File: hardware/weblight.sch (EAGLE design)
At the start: 19 parts, among them U1 ATtiny85-20SU

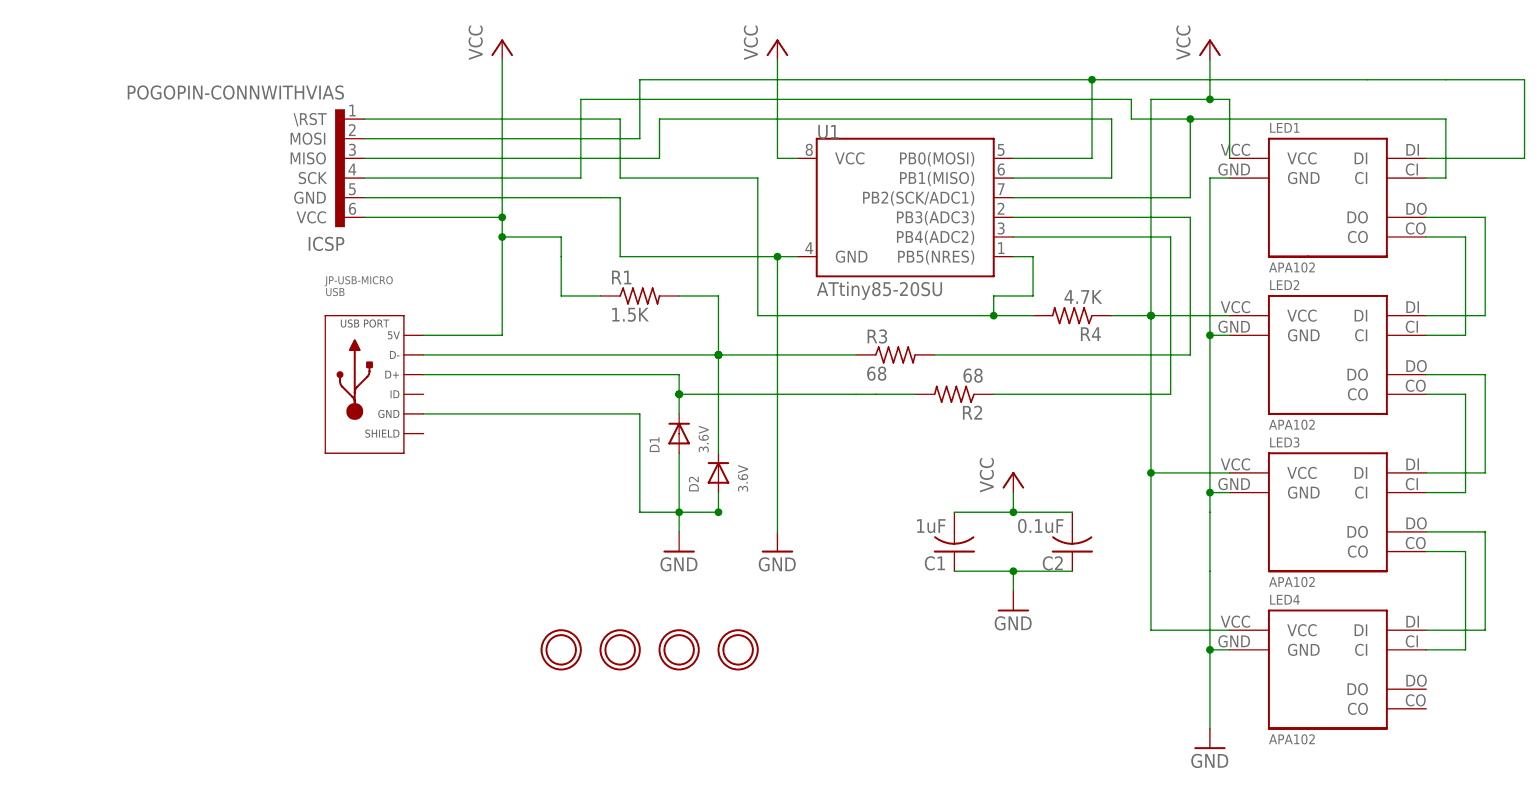
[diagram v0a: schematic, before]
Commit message: mf2 production 0805 - ordered from OSH & Seeed
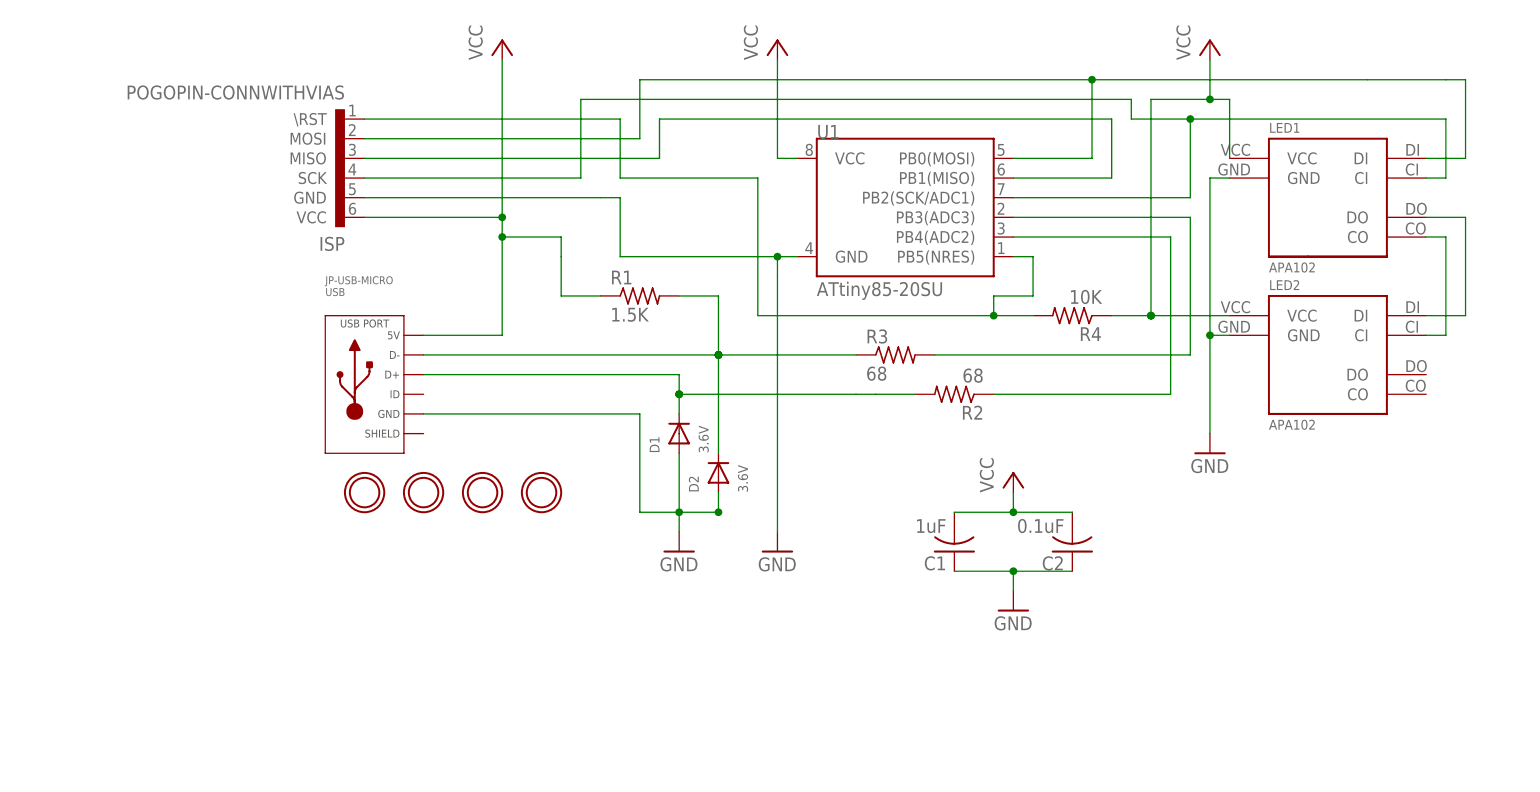
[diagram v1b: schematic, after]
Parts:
- removed LED3, LED4: APA102, weblight:APA102
- C1, C2: device rcl:C-USC0402 -> rcl:C-USC0805
- D1, D2: device microbuilder:DIODESOD-523 -> microbuilder:DIODESOD-323
- R1, R2, R3: device rcl:R-US_R0402 -> rcl:R-US_R0805
- R4: value 4.7K -> 10K; device rcl:R-US_R0402 -> rcl:R-US_R0805
- renumbered ICSP to ISP
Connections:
- removed net CLK_3: LED2.CO, LED3.CI
- removed net CLK_4: LED3.CO, LED4.CI
- removed net DIN_3: LED2.DO, LED3.DI
- removed net DIN_4: LED3.DO, LED4.DI
- net GND: no longer LED3.GND, LED4.GND
- net VCC: no longer LED3.VCC, LED4.VCC

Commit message: Connectorless USB, longer board. Unrouted.
  - Two diodes to protect back connector. Thanks Passerby
    http://electronics.stackexchange.com/q/209941/84391
  - Moved C1/C2 closer to where they matter.
  - A few astute layout changes to facilitate future routing.
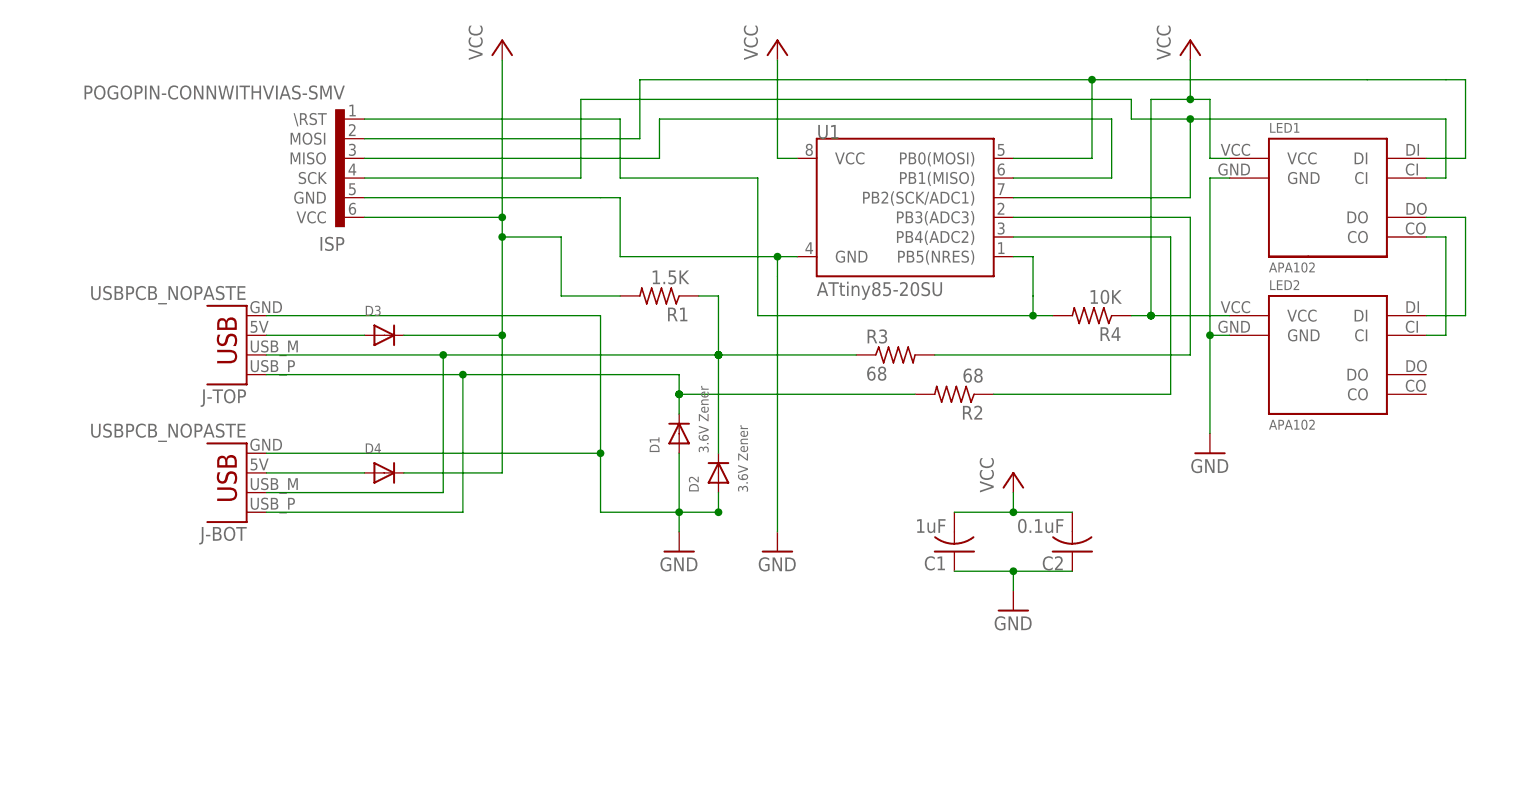
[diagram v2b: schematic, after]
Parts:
- removed HOLE1, HOLE2, HOLE3, HOLE4: MOUNTINGHOLE2.0, microbuilder:MOUNTINGHOLE2.0
- removed JP-USB-MICRO: USB, MF_Connectors:USB_MICRO_RIGHT
- added D3, D4: (no value), microbuilder:DIODESOD-323
- added J-BOT, J-TOP: USBPCB_NOPASTE, SparkFun-Connectors:USBPCB_NOPASTE
- D1, D2: value 3.6V -> 3.6V Zener
- ISP: value POGOPIN-CONNWITHVIAS -> POGOPIN-CONNWITHVIAS-SMV; device weblight:POGOPIN-CONNWITHVIAS -> weblight:POGOPIN-CONNWITHVIAS-SMV
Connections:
- new net 5V: D3.A, D4.A, J-BOT.VBUS, J-TOP.VBUS
- net GND: now also J-BOT.GND, J-TOP.GND; no longer JP-USB-MICRO.GND
- net USB_D_MINUS_RAW: now also J-BOT.D-, J-TOP.D-, R1.1; no longer JP-USB-MICRO.D-, R1.2
- net USB_D_PLUS_RAW: now also J-BOT.D+, J-TOP.D+; no longer JP-USB-MICRO.D+
- net VCC: now also D3.C, D4.C, R1.2; no longer JP-USB-MICRO.5V, R1.1
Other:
- moved on the sheet: R1, R4

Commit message: Mitering
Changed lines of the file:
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@@
 <pinref part="J-TOP" gate="G$1" pin="VBUS"/>
 <pinref part="D3" gate="G$1" pin="A"/>
-<wire x1="-86.36" y1="58.42" x2="-73.66" y2="58.42" width="0.1524" layer="91"/>
-</segment>
-<segment>
+<wire x1="-86.36" y1="58.42" x2="-76.2" y2="58.42" width="0.1524" layer="91"/>
 <pinref part="J-BOT" gate="G$1" pin="VBUS"/>
 <pinref part="D4" gate="G$1" pin="A"/>
-<wire x1="-86.36" y1="40.64" x2="-73.66" y2="40.64" width="0.1524" layer="91"/>
+<wire x1="-76.2" y1="58.42" x2="-73.66" y2="58.42" width="0.1524" layer="91"/>
+<wire x1="-86.36" y1="40.64" x2="-76.2" y2="40.64" width="0.1524" layer="91"/>
+<wire x1="-76.2" y1="40.64" x2="-73.66" y2="40.64" width="0.1524" layer="91"/>
+<wire x1="-76.2" y1="58.42" x2="-76.2" y2="40.64" width="0.1524" layer="91"/>
+<junction x="-76.2" y="58.42"/>
+<junction x="-76.2" y="40.64"/>
 </segment>
 </net>
@@
 </sheet>
 </sheets>
-<errors>
-</errors>
 </schematic>
 </drawing>

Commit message: Routing refinements and re-enabling of diodes
  - Optimized needless turns by embedding them into pads
  - Fixed horrible error that reintroduced short prevented by D3/D4
  - Moved vias away from LED1
  - Shuffled around other vias to stay away from traces
  - Supply LED1 from C1 rather than post-C2
  - Removed bend in C2 trace (magic I don't understand)
  - Fattened up all supply traces
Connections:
- removed net 5V: D3.A, D4.A, J-BOT.VBUS, J-TOP.VBUS
- new net 5V-BOT: D4.A, J-BOT.VBUS
- new net 5V-TOP: D3.A, J-TOP.VBUS
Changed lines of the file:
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@@
 </segment>
 </net>
-<net name="5V" class="0">
+<net name="5V-BOT" class="0">
 <segment>
-<pinref part="J-TOP" gate="G$1" pin="VBUS"/>
-<pinref part="D3" gate="G$1" pin="A"/>
-<wire x1="-86.36" y1="58.42" x2="-76.2" y2="58.42" width="0.1524" layer="91"/>
 <pinref part="J-BOT" gate="G$1" pin="VBUS"/>
 <pinref part="D4" gate="G$1" pin="A"/>
-<wire x1="-76.2" y1="58.42" x2="-73.66" y2="58.42" width="0.1524" layer="91"/>
 <wire x1="-86.36" y1="40.64" x2="-76.2" y2="40.64" width="0.1524" layer="91"/>
 <wire x1="-76.2" y1="40.64" x2="-73.66" y2="40.64" width="0.1524" layer="91"/>
-<wire x1="-76.2" y1="58.42" x2="-76.2" y2="40.64" width="0.1524" layer="91"/>
-<junction x="-76.2" y="58.42"/>
-<junction x="-76.2" y="40.64"/>
 </segment>
 </net>
+<net name="5V-TOP" class="0">
+<segment>
+<pinref part="D3" gate="G$1" pin="A"/>
+<pinref part="J-TOP" gate="G$1" pin="VBUS"/>
+<wire x1="-86.36" y1="58.42" x2="-76.2" y2="58.42" width="0.1524" layer="91"/>
+<wire x1="-76.2" y1="58.42" x2="-73.66" y2="58.42" width="0.1524" layer="91"/>
+</segment>
+</net>

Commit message: Remove tCream from ProtoProg footprint
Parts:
- ISP: value POGOPIN-CONNWITHVIAS-SMV -> POGOPIN-CONN; device weblight:POGOPIN-CONNWITHVIAS-SMV -> weblight:POGOPIN-CONN
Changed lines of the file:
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@@
 <grid distance="0.1" unitdist="inch" unit="inch" style="lines" multiple="1" display="no" altdistance="0.01" altunitdist="inch" altunit="inch"/>
 <layers>
-<layer number="1" name="Top" color="4" fill="1" visible="no" active="no"/>
-<layer number="16" name="Bottom" color="1" fill="1" visible="no" active="no"/>
-<layer number="17" name="Pads" color="2" fill="1" visible="no" active="no"/>
-<layer number="18" name="Vias" color="2" fill="1" visible="no" active="no"/>
-<layer number="19" name="Unrouted" color="6" fill="1" visible="no" active="no"/>
-<layer number="20" name="Dimension" color="15" fill="1" visible="no" active="no"/>
-<layer number="21" name="tPlace" color="7" fill="1" visible="no" active="no"/>
-<layer number="22" name="bPlace" color="7" fill="1" visible="no" active="no"/>
-<layer number="23" name="tOrigins" color="15" fill="1" visible="no" active="no"/>
-<layer number="24" name="bOrigins" color="15" fill="1" visible="no" active="no"/>
-<layer number="25" name="tNames" color="7" fill="1" visible="no" active="no"/>
-<layer number="26" name="bNames" color="7" fill="1" visible="no" active="no"/>
-<layer number="27" name="tValues" color="7" fill="1" visible="no" active="no"/>
-<layer number="28" name="bValues" color="7" fill="1" visible="no" active="no"/>
+<layer number="1" name="Top" color="4" fill="1" visible="yes" active="no"/>
+<layer number="16" name="Bottom" color="1" fill="1" visible="yes" active="no"/>
+<layer number="17" name="Pads" color="2" fill="1" visible="yes" active="no"/>
+<layer number="18" name="Vias" color="2" fill="1" visible="yes" active="no"/>
+<layer number="19" name="Unrouted" color="6" fill="1" visible="yes" active="no"/>
+<layer number="20" name="Dimension" color="15" fill="1" visible="yes" active="no"/>
+<layer number="21" name="tPlace" color="7" fill="1" visible="yes" active="no"/>
+<layer number="22" name="bPlace" color="7" fill="1" visible="yes" active="no"/>
+<layer number="23" name="tOrigins" color="15" fill="1" visible="yes" active="no"/>
+<layer number="24" name="bOrigins" color="15" fill="1" visible="yes" active="no"/>
+<layer number="25" name="tNames" color="7" fill="1" visible="yes" active="no"/>
+<layer number="26" name="bNames" color="7" fill="1" visible="yes" active="no"/>
+<layer number="27" name="tValues" color="7" fill="1" visible="yes" active="no"/>
+<layer number="28" name="bValues" color="7" fill="1" visible="yes" active="no"/>
 <layer number="29" name="tStop" color="7" fill="3" visible="no" active="no"/>
 <layer number="30" name="bStop" color="7" fill="6" visible="no" active="no"/>
@@
 <layer number="35" name="tGlue" color="7" fill="4" visible="no" active="no"/>
 <layer number="36" name="bGlue" color="7" fill="5" visible="no" active="no"/>
-<layer number="37" name="tTest" color="7" fill="1" visible="no" active="no"/>
-<layer number="38" name="bTest" color="7" fill="1" visible="no" active="no"/>
+<layer number="37" name="tTest" color="7" fill="1" visible="yes" active="no"/>
+<layer number="38" name="bTest" color="7" fill="1" visible="yes" active="no"/>
 <layer number="39" name="tKeepout" color="4" fill="11" visible="no" active="no"/>
 <layer number="40" name="bKeepout" color="1" fill="11" visible="no" active="no"/>
@@
 <layer number="44" name="Drills" color="7" fill="1" visible="no" active="no"/>
 <layer number="45" name="Holes" color="7" fill="1" visible="no" active="no"/>
-<layer number="46" name="Milling" color="3" fill="1" visible="no" active="no"/>
-<layer number="47" name="Measures" color="7" fill="1" visible="no" active="no"/>
-<layer number="48" name="Document" color="7" fill="1" visible="no" active="no"/>
-<layer number="49" name="Reference" color="7" fill="1" visible="no" active="no"/>
-<layer number="50" name="dxf" color="7" fill="1" visible="no" active="no"/>
-<layer number="51" name="tDocu" color="7" fill="1" visible="no" active="no"/>
-<layer number="52" name="bDocu" color="7" fill="1" visible="no" active="no"/>
-<layer number="53" name="tGND_GNDA" color="7" fill="9" visible="no" active="no"/>
-<layer number="54" name="bGND_GNDA" color="1" fill="9" visible="no" active="no"/>
-<layer number="56" name="wert" color="7" fill="1" visible="no" active="no"/>
-<layer number="57" name="tCAD" color="7" fill="1" visible="no" active="no"/>
-<layer number="59" name="tCarbon" color="7" fill="1" visible="no" active="no"/>
-<layer number="60" name="bCarbon" color="7" fill="1" visible="no" active="no"/>
+<layer number="46" name="Milling" color="3" fill="1" visible="yes" active="no"/>
+<layer number="47" name="Measures" color="7" fill="1" visible="yes" active="no"/>
+<layer number="48" name="Document" color="7" fill="1" visible="yes" active="no"/>
+<layer number="49" name="Reference" color="7" fill="1" visible="yes" active="no"/>
+<layer number="50" name="dxf" color="7" fill="1" visible="yes" active="no"/>
+<layer number="51" name="tDocu" color="7" fill="1" visible="yes" active="no"/>
+<layer number="52" name="bDocu" color="7" fill="1" visible="yes" active="no"/>
+<layer number="53" name="tGND_GNDA" color="7" fill="9" visible="yes" active="no"/>
+<layer number="54" name="bGND_GNDA" color="1" fill="9" visible="yes" active="no"/>
+<layer number="56" name="wert" color="7" fill="1" visible="yes" active="no"/>
+<layer number="57" name="tCAD" color="7" fill="1" visible="yes" active="no"/>
+<layer number="59" name="tCarbon" color="7" fill="1" visible="yes" active="no"/>
+<layer number="60" name="bCarbon" color="7" fill="1" visible="yes" active="no"/>
 <layer number="90" name="Modules" color="5" fill="1" visible="yes" active="yes"/>
 <layer number="91" name="Nets" color="2" fill="1" visible="yes" active="yes"/>
@@
 <part name="LED1" library="weblight" deviceset="APA102" device=""/>
 <part name="LED2" library="weblight" deviceset="APA102" device=""/>
-<part name="ISP" library="weblight" deviceset="POGOPIN-CONN" device="WITHVIAS-SMV" value="POGOPIN-CONNWITHVIAS-SMV"/>
+<part name="ISP" library="weblight" deviceset="POGOPIN-CONN" device="" value="POGOPIN-CONN"/>
 <part name="J-TOP" library="SparkFun-Connectors" deviceset="USB" device="PCB_NOPASTE"/>
 <part name="J-BOT" library="SparkFun-Connectors" deviceset="USB" device="PCB_NOPASTE"/>
